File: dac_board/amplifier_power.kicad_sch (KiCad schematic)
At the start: 19 parts, among them U1 ADP5071AREZ

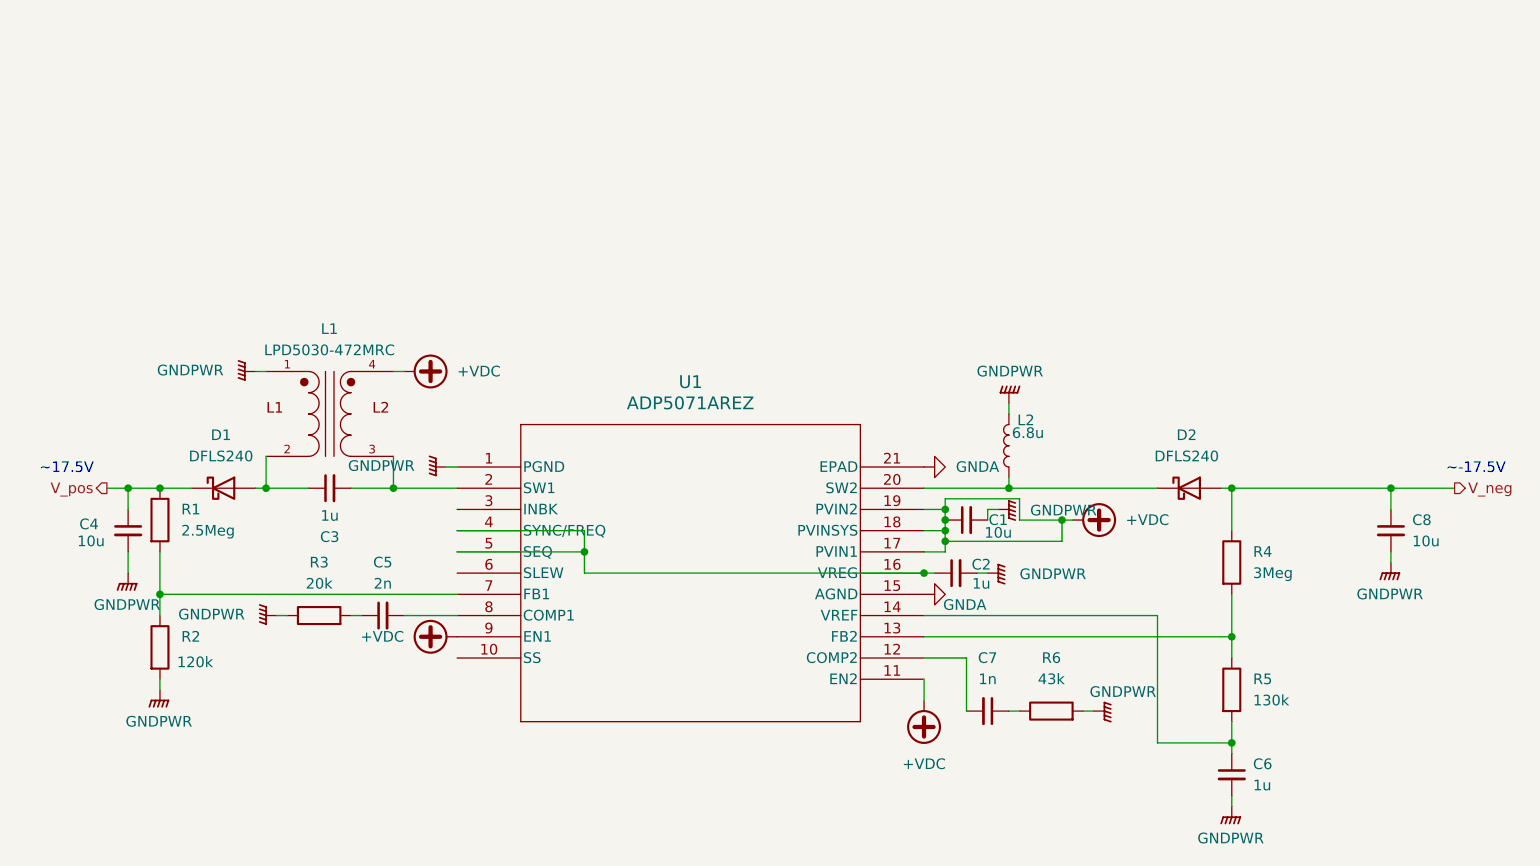
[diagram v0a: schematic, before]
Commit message: Additional work on DAC
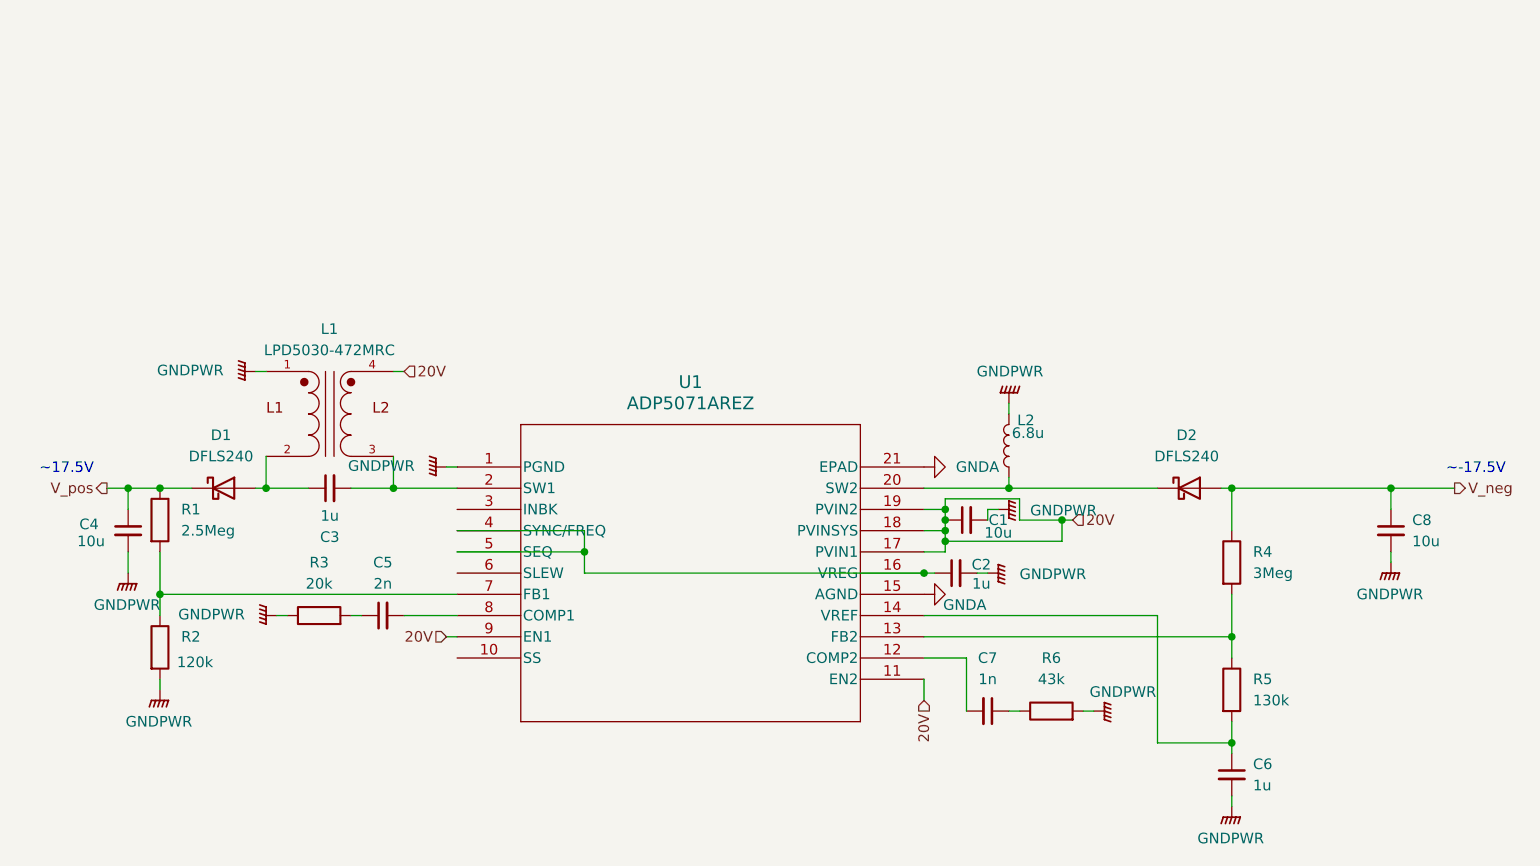
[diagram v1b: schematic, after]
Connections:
- net +VDC renamed 20V

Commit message: More updates, finished DAC block
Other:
- title: (none) -> Amplifier Power Supply
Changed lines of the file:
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@@
 	(generator_version "9.0")
 	(paper "A4")
+	(title_block
+		(title "Amplifier Power Supply")
+	)
 	(text "~-17.5V"
 		(exclude_from_sim no)

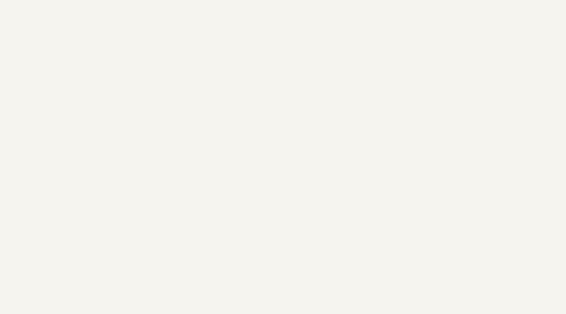
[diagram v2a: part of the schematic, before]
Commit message: Finished schematic design for MCU + DAC
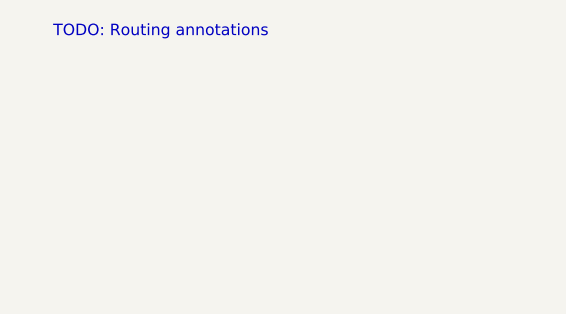
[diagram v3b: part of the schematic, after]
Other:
- note added: "TODO: Routing annotations"
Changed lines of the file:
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@@
 		(title "Amplifier Power Supply")
+	)
+	(text "TODO: Routing annotations"
+		(exclude_from_sim no)
+		(at 87.63 26.416 0)
+		(effects
+			(font
+				(size 1.27 1.27)
+			)
+		)
 	)
 	(text "~-17.5V"
